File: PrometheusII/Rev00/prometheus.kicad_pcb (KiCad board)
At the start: 4 copper layers, 223.5 x 222.3 mm, 196 parts, among them J1 0878311420, J10 Conn_02x02_Odd_Even, J11 Conn_02x02_Odd_Even, J16 Conn_02x07_Odd_Even, J17 Conn_02x07_Odd_Even, J18 Conn_02x07_Odd_Even, J19 Conn_02x07_Odd_Even, J2 Conn_02x08_Odd_Even, J3 Conn_02x02_Odd_Even, J4 Conn_02x02_Odd_Even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

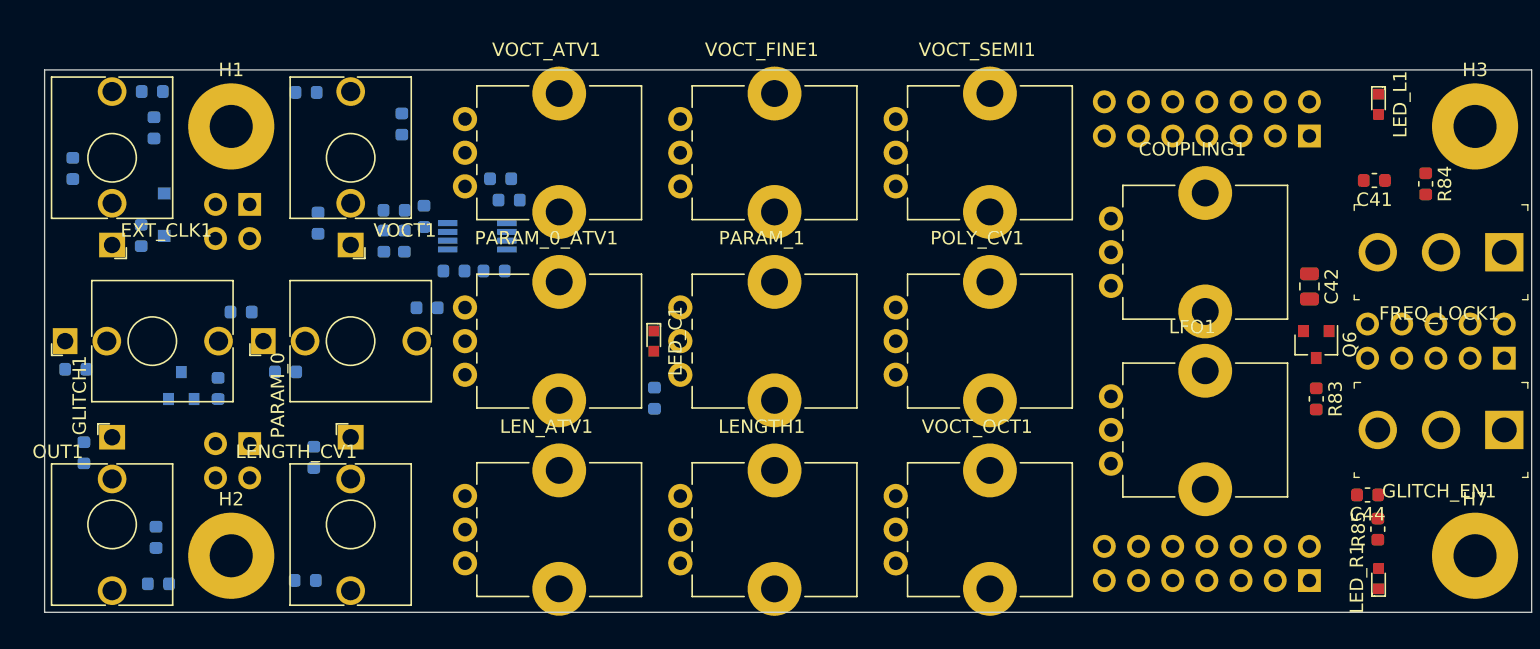
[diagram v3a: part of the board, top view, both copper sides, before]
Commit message: controls board placement finished
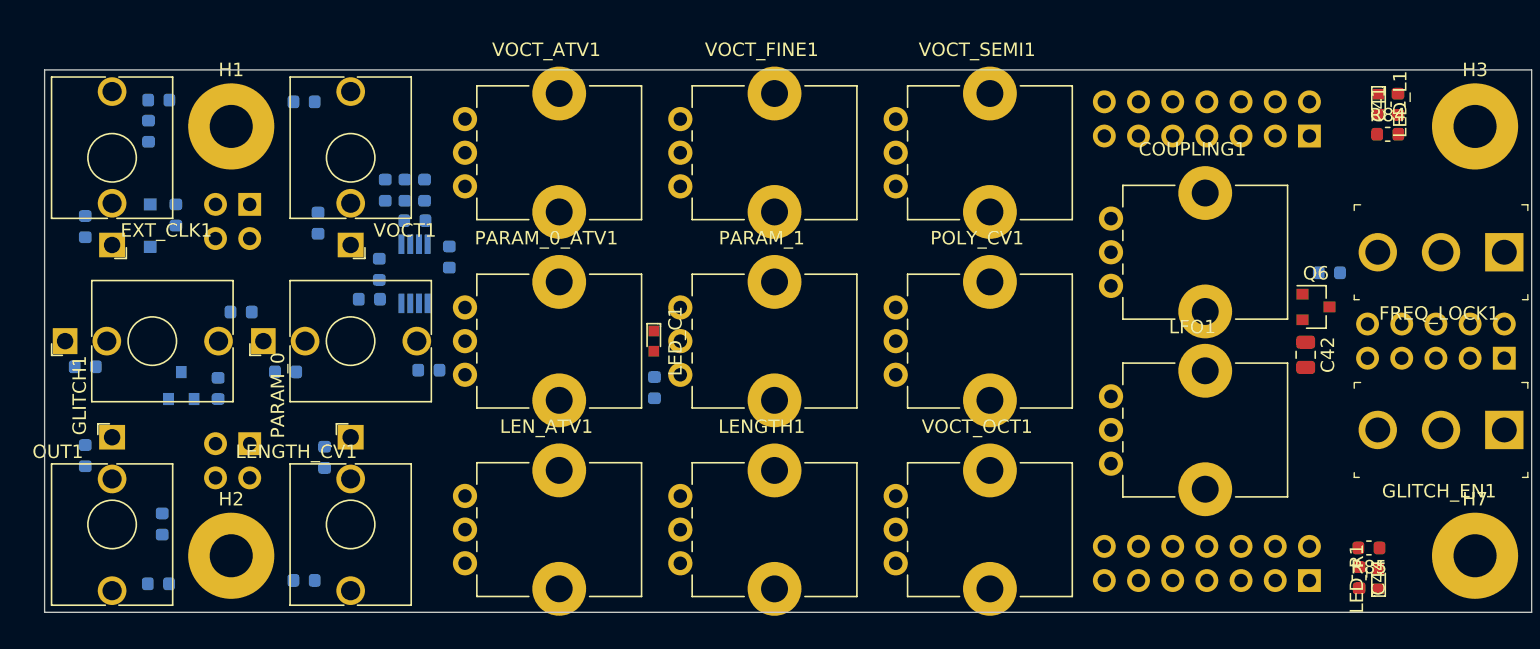
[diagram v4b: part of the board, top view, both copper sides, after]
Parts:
- removed R77, R80: 0, Resistor_SMD:R_0603_1608Metric
- D1, D12, D2: value D -> SD0603S040S0R2
- R83: moved to B.Cu
- moved R83 9.42 mm to (112.0, 104.1), turned to 0 degrees
- moved D10 8.16 mm to (25.0, 91.3), turned to 0 degrees
- moved R58 7.38 mm to (40.6, 106.1), turned to 180 degrees
- moved D12 6.68 mm to (26.3, 99.8)
- moved C44 6.17 mm to (114.2, 126.8), turned to 270 degrees
- moved C41 5.92 mm to (117.1, 91.6), turned to 90 degrees
- moved R53 5.55 mm to (41.4, 103.9), turned to 90 degrees
- moved U9 5.43 mm to (44.0, 104.2), turned to 90 degrees
- moved C42 5.09 mm to (110.2, 110.2)
- moved R57 5.07 mm to (41.8, 98.0)
- moved R66 4.84 mm to (44.7, 98.0)
- moved R84 4.64 mm to (116.3, 93.9), turned to 0 degrees
- moved D6 4.64 mm to (45.1, 111.4)
- moved R47 4.21 mm to (19.5, 100.7)
- moved C37 3.49 mm to (46.6, 103.0), turned to 90 degrees
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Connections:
- U9 pad 1: Net-(C35-Pad2) -> Net-(U9-Pad1)
- U9 pad 2: Net-(C35-Pad1) -> Net-(U9-Pad1)
- U9 pad 5: Net-(R77-Pad2) -> Net-(R53-Pad1)
- U9 pad 6: Net-(R80-Pad2) -> Net-(C35-Pad1)
- U9 pad 7: Net-(R80-Pad1) -> Net-(C35-Pad2)

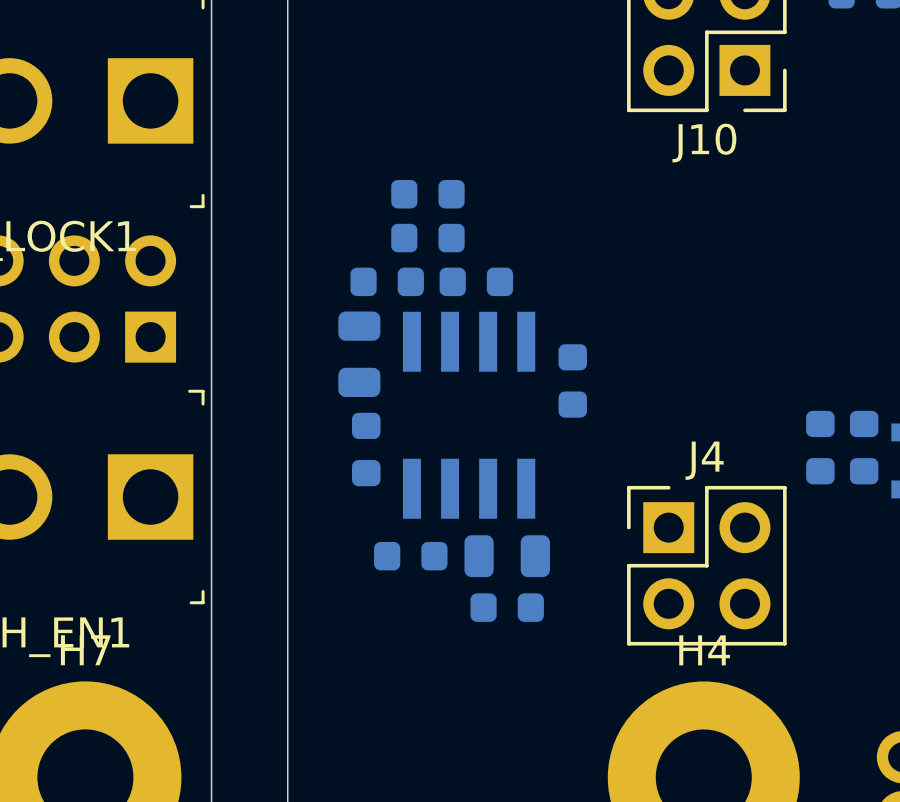
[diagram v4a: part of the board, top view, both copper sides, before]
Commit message: Fixed oversized footprint
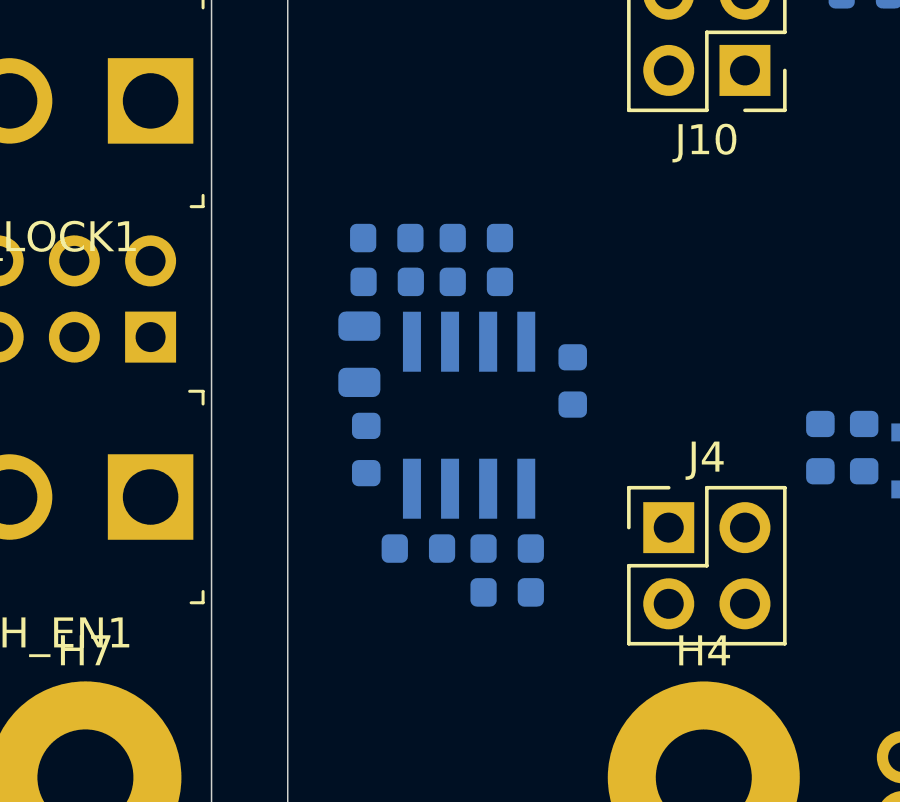
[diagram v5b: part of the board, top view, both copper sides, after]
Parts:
- C24: footprint Capacitor_SMD:C_0805_2012Metric -> Capacitor_SMD:C_0603_1608Metric
- moved R81 2.00 mm to (132.8, 107.2)
- moved R22 1.61 mm to (135.8, 107.2), turned to 0 degrees
- moved R32 0.51 mm to (136.9, 119.0)
- moved R27 0.36 mm to (133.9, 117.5)
- moved C24 0.25 mm to (136.9, 117.5)

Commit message: checkpoint
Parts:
- moved C31 20.7 mm to (178.5, 98.9)
- moved C32 20.7 mm to (178.5, 104.2)
- moved R41 20.7 mm to (177.5, 97.4)
- moved U6 20.7 mm to (177.7, 101.6)
- moved C30 1.08 mm to (168.9, 98.1), turned to 270 degrees
- moved D3 0.94 mm to (166.9, 100.5)
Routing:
- net GND: track 10.3 -> 629.5 mm
- net -12V: track 0.00 -> 1.14 mm, vias 0 -> 4
- net +12V: vias 0 -> 4
- net (no net): vias 0 -> 6

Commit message: checkpoint
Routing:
- net -12V: track 1.14 -> 32.8 mm, vias 4 -> 6
- net +12V: track 0.00 -> 30.8 mm, vias 4 -> 6
- net GND: track 629.5 -> 624.3 mm
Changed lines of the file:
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@@
     (thickness 1.6)
     (drawings 40)
-    (tracks 139)
+    (tracks 149)
     (zones 0)
     (modules 194)
@@
   )
   (setup
-    (last_trace_width 0.4)
+    (last_trace_width 0.3)
     (user_trace_width 0.15)
     (user_trace_width 0.1524)
@@
   (segment (start 144.78 119.38) (end 143.4084 125.168) (width 0.3) (layer In1.Cu) (net 1))
   (segment (start 159.662 97.409) (end 158.445915 99.733915) (width 0.3) (layer In1.Cu) (net 1))
-  (segment (start 131.737 113.284) (end 139.0395 112.649) (width 0.3) (layer In1.Cu) (net 1))
-  (segment (start 139.0395 112.649) (end 158.445915 99.733915) (width 0.3) (layer In1.Cu) (net 1))
   (segment (start 158.445915 99.733915) (end 144.78 101.6) (width 0.3) (layer In1.Cu) (net 1))
   (segment (start 144.78 116.84) (end 158.445915 99.733915) (width 0.3) (layer In1.Cu) (net 1))
@@
   (segment (start 163.6775 125.857) (end 163.868 123.444) (width 0.3) (layer In1.Cu) (net 1))
   (segment (start 208.28 91.43) (end 182.2195 90.6145) (width 0.3) (layer In1.Cu) (net 1))
-  (segment (start 166.916 99.822) (end 164.111663 99.895837) (width 0.3) (layer F.Cu) (net 1))
   (segment (start 161.3535 92.964) (end 162.979 90.297) (width 0.3) (layer In1.Cu) (net 1))
   (segment (start 162.979 90.297) (end 163.6775 90.1065) (width 0.3) (layer In1.Cu) (net 1))
   (segment (start 163.6775 90.1065) (end 182.2195 90.6145) (width 0.3) (layer In1.Cu) (net 1))
-  (segment (start 166.916 99.822) (end 168.948 99.045) (width 0.3) (layer F.Cu) (net 1))
   (segment (start 198.4502 123.0376) (end 184.696 114.173) (width 0.3) (layer In1.Cu) (net 1))
   (segment (start 184.696 114.173) (end 182.283 114.1095) (width 0.3) (layer In1.Cu) (net 1))
-  (segment (start 163.965466 99.661034) (end 164.111663 99.895837) (width 0.3) (layer F.Cu) (net 1))
   (segment (start 182.41 111.4425) (end 182.205583 111.329417) (width 0.3) (layer In1.Cu) (net 1))
   (segment (start 168.948 99.045) (end 182.205583 111.329417) (width 0.3) (layer In1.Cu) (net 1))
@@
   (segment (start 227.844 110.492) (end 198.4502 123.0376) (width 0.3) (layer In1.Cu) (net 1))
   (segment (start 164.249458 99.885042) (end 182.41 111.4425) (width 0.3) (layer In1.Cu) (net 1))
-  (segment (start 164.249458 99.885042) (end 163.965466 99.661034) (width 0.3) (layer F.Cu) (net 1))
   (segment (start 182.283 114.1095) (end 164.249458 99.885042) (width 0.3) (layer In1.Cu) (net 1))
   (segment (start 184.442 111.887) (end 197.3325 119.0625) (width 0.3) (layer In1.Cu) (net 1))
@@
   (segment (start 200.1265 119.253) (end 225.59 116.7765) (width 0.3) (layer In1.Cu) (net 1))
   (segment (start 225.59 116.7765) (end 225.971 119.888) (width 0.3) (layer In1.Cu) (net 1))
+  (segment (start 140.9445 112.776) (end 158.445915 99.733915) (width 0.3) (layer In1.Cu) (net 1))
+  (segment (start 131.737 113.284) (end 140.9445 112.776) (width 0.3) (layer In1.Cu) (net 1))
+  (via (at 140.119 110.8075) (size 0.508) (drill 0.254) (layers F.Cu B.Cu) (net 2))
+  (via (at 140.119 111.506) (size 0.508) (drill 0.254) (layers F.Cu B.Cu) (net 2))
+  (segment (start 140.119 111.506) (end 140.119 110.8075) (width 0.3) (layer B.Cu) (net 2))
+  (segment (start 154.393363 104.253863) (end 156.0575 101.5365) (width 0.3) (layer F.Cu) (net 2))
+  (segment (start 154.393363 104.253863) (end 140.119 110.8075) (width 0.3) (layer F.Cu) (net 2))
+  (segment (start 154.56744 104.17394) (end 154.393363 104.253863) (width 0.3) (layer F.Cu) (net 2))
+  (segment (start 156.0575 101.5365) (end 156.756 100.584) (width 0.3) (layer F.Cu) (net 2))
+  (segment (start 156.756 100.584) (end 166.4335 98.726) (width 0.3) (layer F.Cu) (net 2))
   (via (at 157.391 98.552) (size 0.508) (drill 0.254) (layers F.Cu B.Cu) (net 3))
   (segment (start 157.787 97.409) (end 157.772 98.552) (width 0.3) (layer F.Cu) (net 3))
+  (segment (start 156.2735 98.726) (end 153.8985 103.5685) (width 0.3) (layer F.Cu) (net 3))
+  (segment (start 153.8985 103.5685) (end 137.5155 110.6805) (width 0.3) (layer F.Cu) (net 3))
+  (via (at 130.9115 114.6175) (size 0.508) (drill 0.254) (layers F.Cu B.Cu) (net 3))
+  (segment (start 137.5155 110.6805) (end 130.9115 114.6175) (width 0.3) (layer F.Cu) (net 3))
+  (via (at 130.9115 115.3795) (size 0.508) (drill 0.254) (layers F.Cu B.Cu) (net 3))
+  (segment (start 130.9115 115.3795) (end 130.9115 114.6175) (width 0.3) (layer F.Cu) (net 3))
   (segment (start 175.799999 122.040999) (end 176.3395 122.5805) (width 0.1524) (layer B.Cu) (net 6))
   (segment (start 174.846501 122.040999) (end 175.799999 122.040999) (width 0.1524) (layer B.Cu) (net 6))

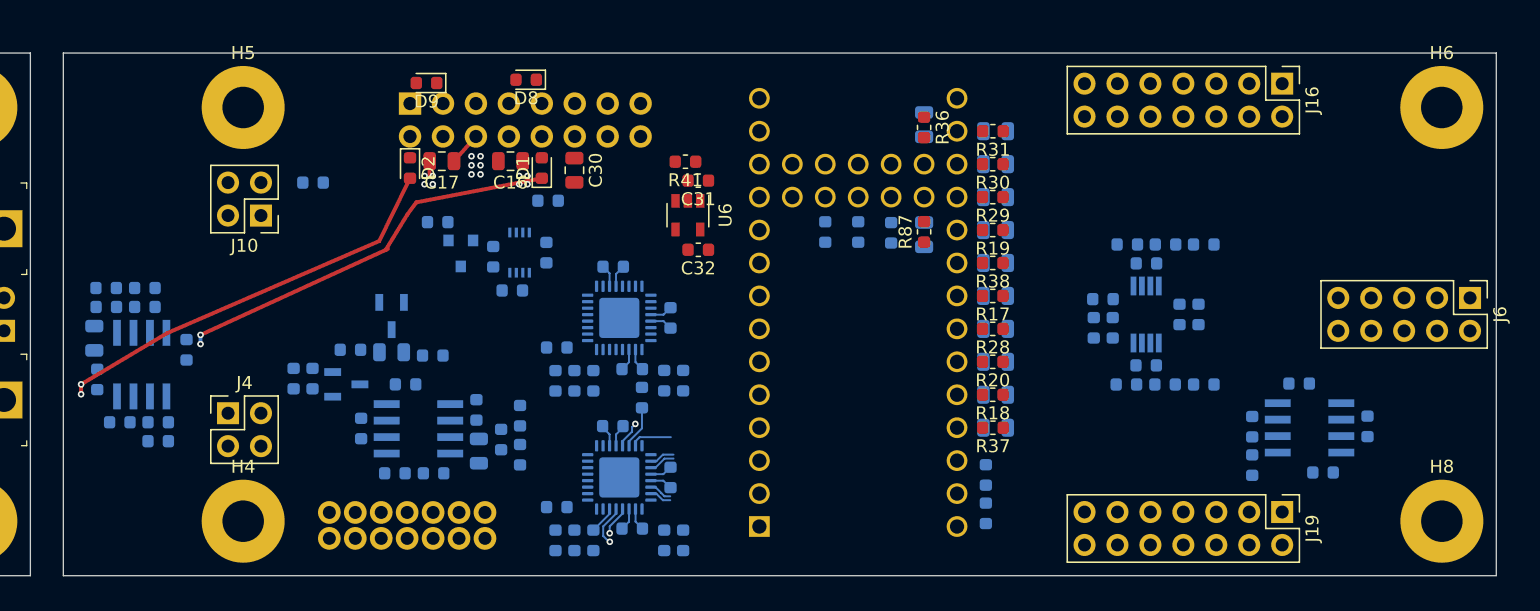
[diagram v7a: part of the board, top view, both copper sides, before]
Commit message: main board top section signal routing
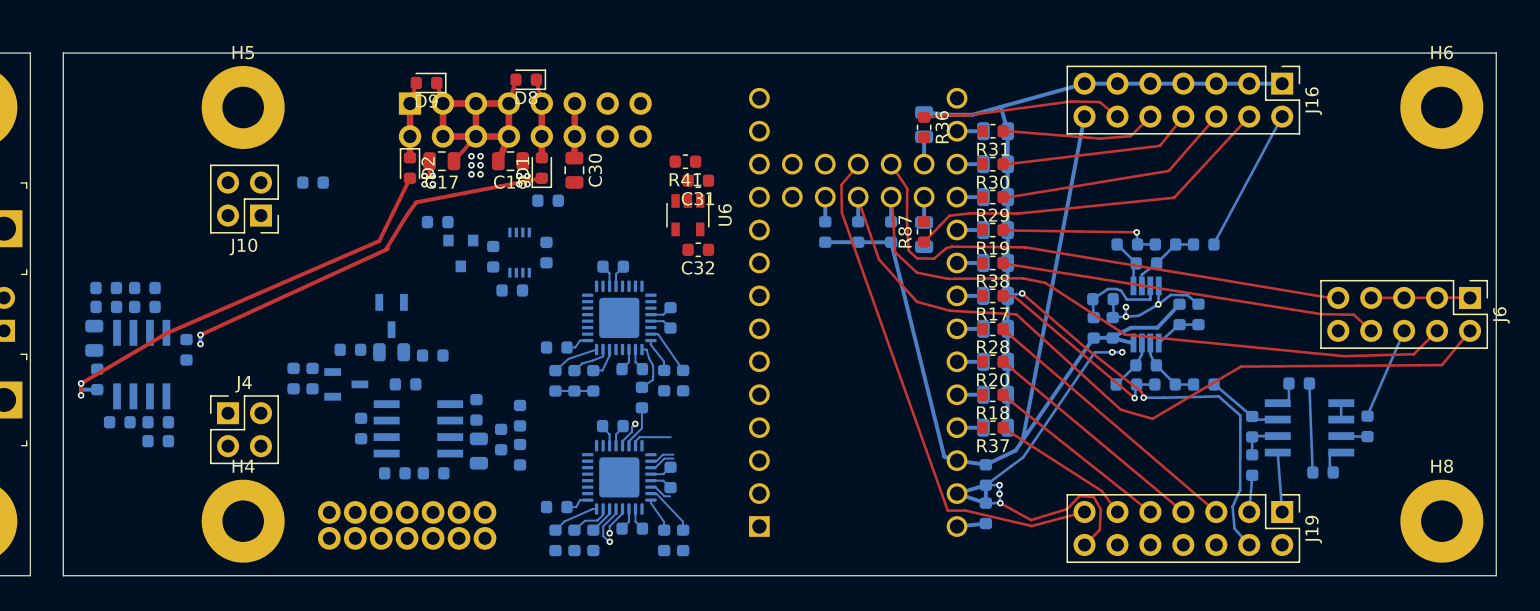
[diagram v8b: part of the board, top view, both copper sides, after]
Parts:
- moved R59 0.06 mm to (193.4, 102.9)
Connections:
- J2 pad 14: Net-(J2-Pad13) -> Net-(J2-Pad14)
- J2 pad 16: Net-(J2-Pad15) -> Net-(J2-Pad16)
- J5 pad 1: GND -> /FREQ_LOCK_P
- J5 pad 2: /FREQ_LOCK_P -> GND
- J5 pad 5: GND -> /CV_FILT_P
- J5 pad 6: /CV_FILT_P -> GND
- J6 pad 1: /FREQ_LOCK_T -> GND
- J6 pad 2: GND -> /FREQ_LOCK_T
- J6 pad 5: /_CV_FILT -> GND
- J6 pad 6: GND -> /_CV_FILT
- R52 pad 1: /GLITCH_IN_T -> /FREQ_LOCK_T
- R67 pad 1: /FREQ_LOCK_T -> /GLITCH_IN_T
- U1 pad 36: /TAPS_LED_T -> /LFO_LED_T
- U1 pad 37: /LFO_LED_T -> /TAPS_LED_T
- U1 pad 42: /GLITCH_IN_T -> /FREQ_LOCK_T
- U1 pad 43: /FREQ_LOCK_T -> /GLITCH_IN_T
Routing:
- net GND: track 624.3 -> 788.1 mm, vias 0 -> 10
- net +3V3: track 6.85 -> 80.0 mm
- net /FREQ_LOCK_T: track 0.00 -> 59.4 mm
- net /GLITCH_EN_T: track 0.00 -> 50.8 mm
- net /LFO_LED_T: track 0.00 -> 41.1 mm
- net /TAPS_LED_T: track 0.00 -> 39.4 mm
- net /LFO: track 0.00 -> 29.2 mm
- net /PARAM_0: track 0.00 -> 28.7 mm
- net /POLY: track 0.00 -> 21.8 mm
- net /VOCT_CV: track 0.00 -> 18.5 mm
- net /PARAM_1: track 0.00 -> 18.1 mm
- net /VOCT_SEMI: track 0.00 -> 15.4 mm
- net /LEN_CV: track 0.00 -> 15.4 mm, vias 0 -> 1
- net /VOCT_ATV: track 0.00 -> 14.9 mm
- net /LEN_KNOB: track 0.00 -> 14.6 mm
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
